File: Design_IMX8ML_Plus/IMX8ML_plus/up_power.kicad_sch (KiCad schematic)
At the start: 1 part, among them U1 MIMX8ML8CVNKZAB

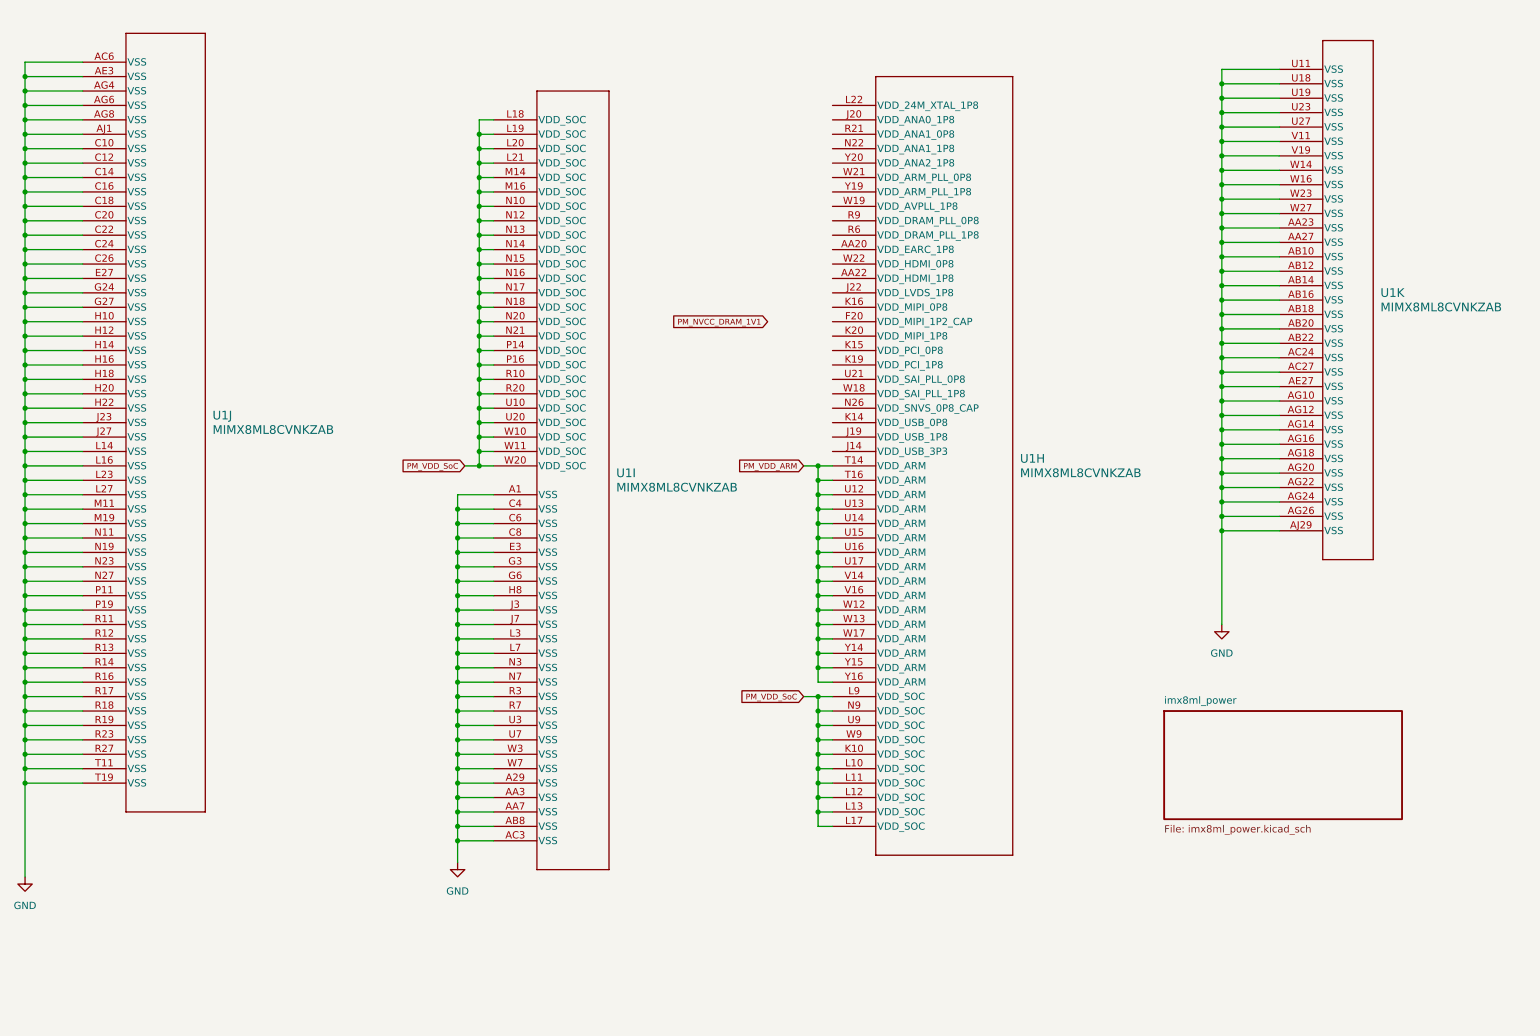
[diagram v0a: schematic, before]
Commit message: Add storage unit
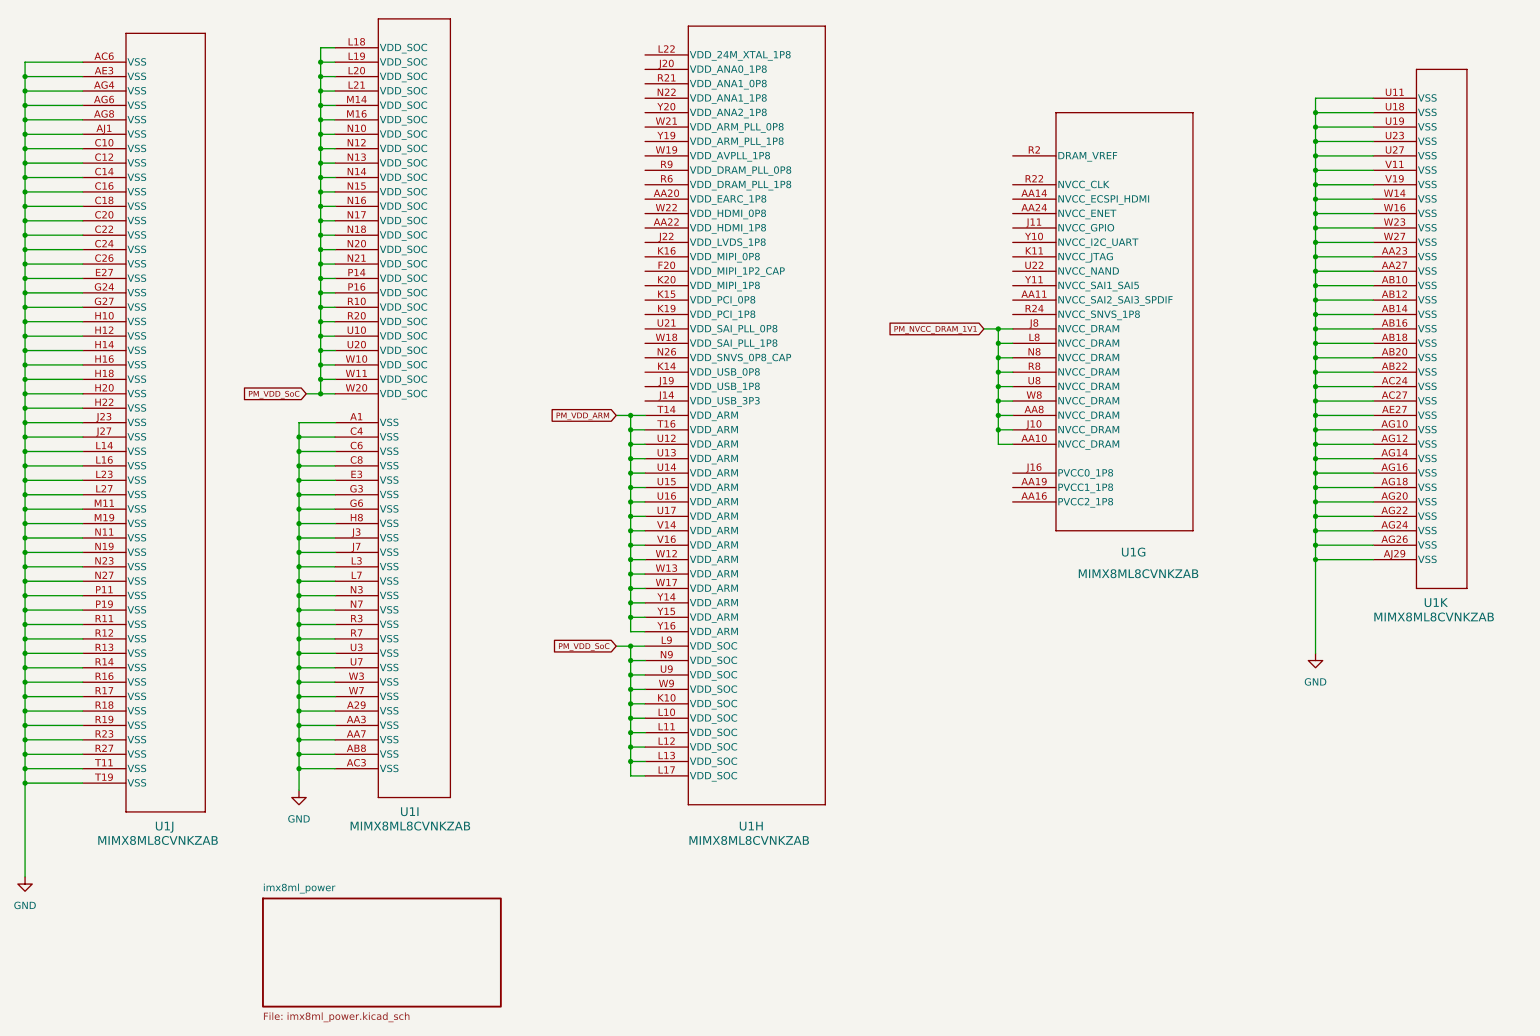
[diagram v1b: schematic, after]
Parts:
- added unit 7 of U1
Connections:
- net PM_NVCC_DRAM_1V1: now also U1.AA10 (NVCC_DRAM), U1.AA8 (NVCC_DRAM), U1.J10 (NVCC_DRAM), U1.J8 (NVCC_DRAM), U1.L8 (NVCC_DRAM), U1.N8 (NVCC_DRAM), U1.R8 (NVCC_DRAM), U1.U8 (NVCC_DRAM), U1.W8 (NVCC_DRAM)
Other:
- moved on the sheet: U1H, U1I, U1K

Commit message: Add interface io pins
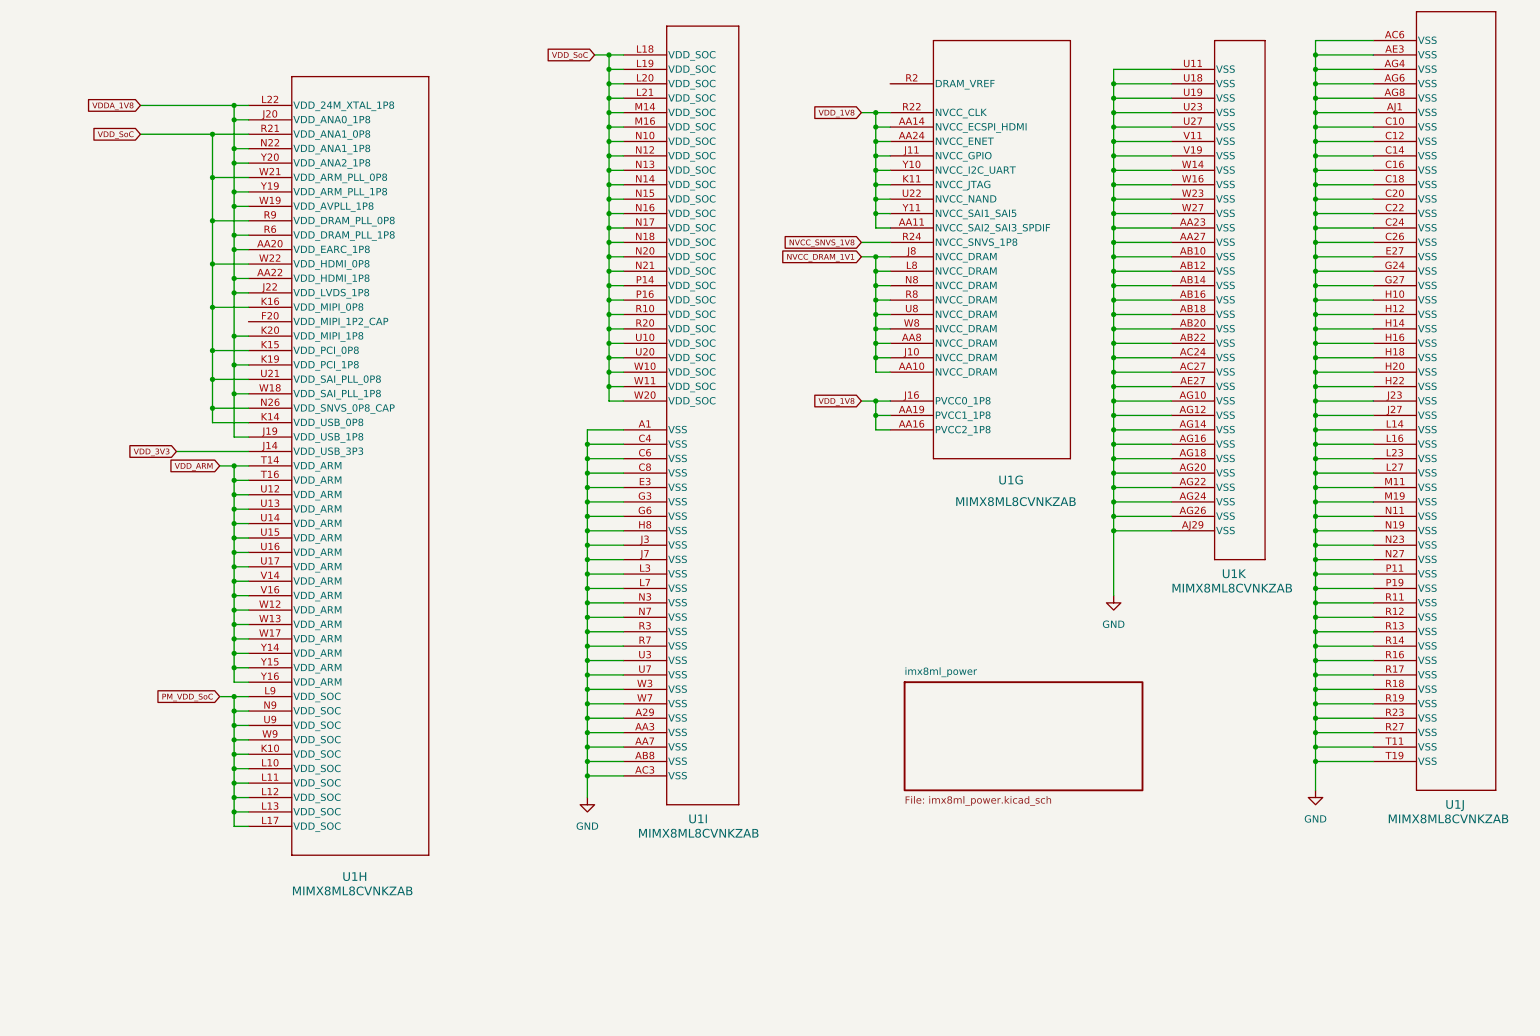
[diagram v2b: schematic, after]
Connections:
- net PM_VDD_SoC: no longer U1.L18 (VDD_SOC), U1.L19 (VDD_SOC), U1.L20 (VDD_SOC), U1.L21 (VDD_SOC), U1.M14 (VDD_SOC), U1.M16 (VDD_SOC), U1.N10 (VDD_SOC), U1.N12 (VDD_SOC), U1.N13 (VDD_SOC), U1.N14 (VDD_SOC), U1.N15 (VDD_SOC), U1.N16 (VDD_SOC), U1.N17 (VDD_SOC), U1.N18 (VDD_SOC), U1.N20 (VDD_SOC), U1.N21 (VDD_SOC), U1.P14 (VDD_SOC), U1.P16 (VDD_SOC), U1.R10 (VDD_SOC), U1.R20 (VDD_SOC), U1.U10 (VDD_SOC), U1.U20 (VDD_SOC), U1.W10 (VDD_SOC), U1.W11 (VDD_SOC), U1.W20 (VDD_SOC)
- net VDD_1V8: now reaches U1.AA11 (NVCC_SAI2_SAI3_SPDIF)
- net VDD_1V8: now also U1.AA14 (NVCC_ECSPI_HDMI), U1.AA16 (PVCC2_1P8), U1.AA19 (PVCC1_1P8), U1.AA24 (NVCC_ENET), U1.J11 (NVCC_GPIO), U1.J16 (PVCC0_1P8), U1.K11 (NVCC_JTAG), U1.R22 (NVCC_CLK), U1.U22 (NVCC_NAND), U1.Y10 (NVCC_I2C_UART), U1.Y11 (NVCC_SAI1_SAI5)
- net NVCC_SNVS_1V8: now reaches U1.R24 (NVCC_SNVS_1P8)
- net VDDA_1V8: now reaches U1.AA20 (VDD_EARC_1P8)
- net VDDA_1V8: now also U1.AA22 (VDD_HDMI_1P8), U1.J19 (VDD_USB_1P8), U1.J20 (VDD_ANA0_1P8), U1.J22 (VDD_LVDS_1P8), U1.K19 (VDD_PCI_1P8), U1.K20 (VDD_MIPI_1P8), U1.L22 (VDD_24M_XTAL_1P8), U1.N22 (VDD_ANA1_1P8), U1.R6 (VDD_DRAM_PLL_1P8), U1.W18 (VDD_SAI_PLL_1P8), U1.W19 (VDD_AVPLL_1P8), U1.Y19 (VDD_ARM_PLL_1P8), U1.Y20 (VDD_ANA2_1P8)
- net VDD_3V3: now reaches U1.J14 (VDD_USB_3P3)
- net VDD_SoC: now reaches U1.K14 (VDD_USB_0P8)
- net VDD_SoC: now also U1.K15 (VDD_PCI_0P8), U1.K16 (VDD_MIPI_0P8), U1.L18 (VDD_SOC), U1.L19 (VDD_SOC), U1.L20 (VDD_SOC), U1.L21 (VDD_SOC), U1.M14 (VDD_SOC), U1.M16 (VDD_SOC), U1.N10 (VDD_SOC), U1.N12 (VDD_SOC), U1.N13 (VDD_SOC), U1.N14 (VDD_SOC), U1.N15 (VDD_SOC), U1.N16 (VDD_SOC), U1.N17 (VDD_SOC), U1.N18 (VDD_SOC), U1.N20 (VDD_SOC), U1.N21 (VDD_SOC), U1.N26 (VDD_SNVS_0P8_CAP), U1.P14 (VDD_SOC), U1.P16 (VDD_SOC), U1.R10 (VDD_SOC), U1.R20 (VDD_SOC), U1.R21 (VDD_ANA1_0P8), U1.R9 (VDD_DRAM_PLL_0P8), U1.U10 (VDD_SOC), U1.U20 (VDD_SOC), U1.U21 (VDD_SAI_PLL_0P8), U1.W10 (VDD_SOC), U1.W11 (VDD_SOC), U1.W20 (VDD_SOC), U1.W21 (VDD_ARM_PLL_0P8), U1.W22 (VDD_HDMI_0P8)
- net PM_NVCC_DRAM_1V1 renamed NVCC_DRAM_1V1
- net PM_VDD_ARM renamed VDD_ARM
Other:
- moved on the sheet: U1G, U1H, U1I, U1J, U1K

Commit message: [PROCESSOR] Create zones It added power zones in the four layer
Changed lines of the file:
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@@
 	(wire
 		(pts
-			(xy 49.53 90.17) (xy 62.23 90.17)
+			(xy 57.15 90.17) (xy 62.23 90.17)
 		)
 		(stroke
@@
 	(global_label "VDD_3V3"
 		(shape input)
-		(at 49.53 90.17 180)
+		(at 57.15 90.17 180)
 		(fields_autoplaced yes)
 		(effects
@@
 		)
 		(property "Intersheetrefs" "${INTERSHEET_REFS}"
-			(at 40.8612 90.17 0)
+			(at 48.4812 90.17 0)
 			(effects
 				(font
@@
 		(dnp no)
 		(fields_autoplaced yes)
-		(property "Reference" "#PWR02"
+		(property "Reference" "#PWR3"
 			(at 250.19 156.21 0)
 			(effects
@@
 			(project "IMX8ML_plus"
 				(path "/1e0dca60-79b3-4b5b-ab8f-7b2adbc68a5f/c2b8be6d-439a-444c-a168-f4e9f22d3fc9/ff1e19bc-8af5-40c7-aebc-3ecef7e734aa"
-					(reference "#PWR02")
+					(reference "#PWR3")
 					(unit 1)
 				)
@@
 		(dnp no)
 		(fields_autoplaced yes)
-		(property "Reference" "#PWR03"
+		(property "Reference" "#PWR1"
 			(at 121.92 157.48 0)
 			(effects
@@
 			(project "IMX8ML_plus"
 				(path "/1e0dca60-79b3-4b5b-ab8f-7b2adbc68a5f/c2b8be6d-439a-444c-a168-f4e9f22d3fc9/ff1e19bc-8af5-40c7-aebc-3ecef7e734aa"
-					(reference "#PWR03")
+					(reference "#PWR1")
 					(unit 1)
 				)
@@
 		(dnp no)
 		(fields_autoplaced yes)
-		(property "Reference" "#PWR01"
+		(property "Reference" "#PWR2"
 			(at 214.63 121.92 0)
 			(effects
@@
 			(project "IMX8ML_plus"
 				(path "/1e0dca60-79b3-4b5b-ab8f-7b2adbc68a5f/c2b8be6d-439a-444c-a168-f4e9f22d3fc9/ff1e19bc-8af5-40c7-aebc-3ecef7e734aa"
-					(reference "#PWR01")
+					(reference "#PWR2")
 					(unit 1)
 				)

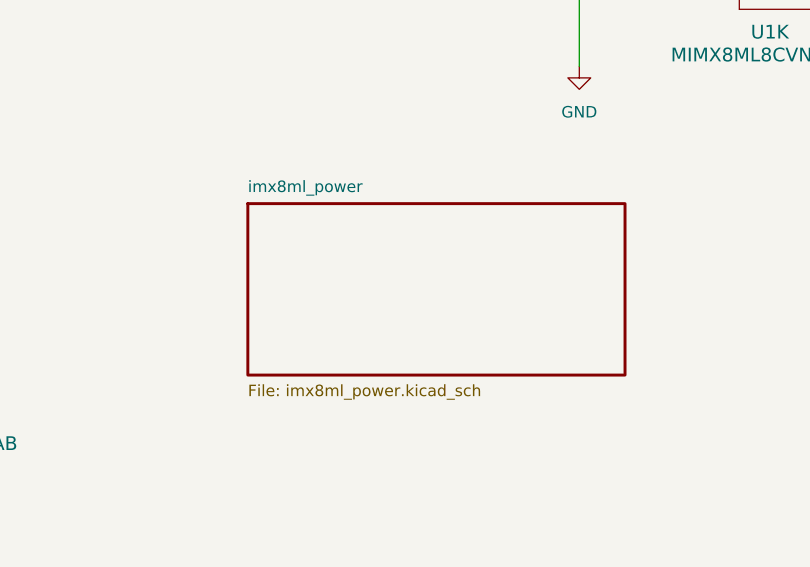
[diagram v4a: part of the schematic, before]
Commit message: [BB_IMX8MLP IMX8MLP] Actuallizated to 9.0 kicad version
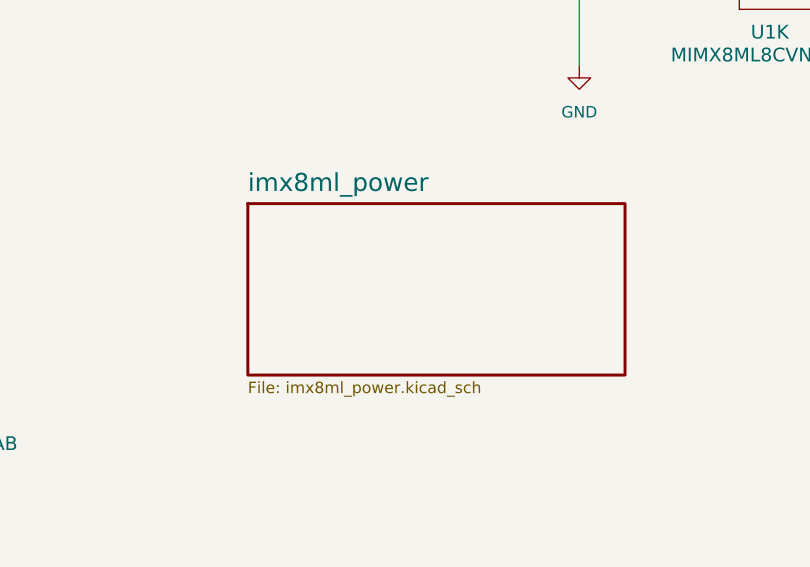
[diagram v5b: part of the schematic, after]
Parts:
- U1: footprint LFBGA548_SOT2047-1_NXP -> _W_SBC:LFBGA548_SOT2047-1_NXP; MP (none) -> -
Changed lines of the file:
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@@
 (kicad_sch
-	(version 20231120)
+	(version 20250114)
 	(generator "eeschema")
-	(generator_version "8.0")
+	(generator_version "9.0")
 	(paper "A4")
 	(junction
@@
 			)
 		)
-		(property "Footprint" "LFBGA548_SOT2047-1_NXP"
+		(property "Footprint" "_W_SBC:LFBGA548_SOT2047-1_NXP"
 			(at 265.43 22.86 0)
 			(effects
@@
 			)
 		)
+		(property "MP" "-"
+			(at 224.79 22.86 0)
+			(effects
+				(font
+					(size 1.27 1.27)
+				)
+				(hide yes)
+			)
+		)
 		(pin "F8"
 		)
@@
 			)
 		)
-		(property "Footprint" "LFBGA548_SOT2047-1_NXP"
+		(property "Footprint" "_W_SBC:LFBGA548_SOT2047-1_NXP"
 			(at 300.99 17.78 0)
 			(effects
@@
 			)
 		)
+		(property "MP" "-"
+			(at 260.35 17.78 0)
+			(effects
+				(font
+					(size 1.27 1.27)
+				)
+				(hide yes)
+			)
+		)
 		(pin "F8"
 		)
@@
 			)
 		)
-		(property "Footprint" "LFBGA548_SOT2047-1_NXP"
+		(property "Footprint" "_W_SBC:LFBGA548_SOT2047-1_NXP"
 			(at 215.9 25.4 0)
 			(effects
@@
 			)
 		)
+		(property "MP" "-"
+			(at 175.26 25.4 0)
+			(effects
+				(font
+					(size 1.27 1.27)
+				)
+				(hide yes)
+			)
+		)
 		(pin "F8"
 		)
@@
 			)
 		)
-		(property "Footprint" "LFBGA548_SOT2047-1_NXP"
+		(property "Footprint" "_W_SBC:LFBGA548_SOT2047-1_NXP"
 			(at 102.87 29.21 0)
 			(effects
@@
 			)
 		)
+		(property "MP" "-"
+			(at 62.23 29.21 0)
+			(effects
+				(font
+					(size 1.27 1.27)
+				)
+				(hide yes)
+			)
+		)
 		(pin "F8"
 		)
@@
 			)
 		)
-		(property "Footprint" "LFBGA548_SOT2047-1_NXP"
+		(property "Footprint" "_W_SBC:LFBGA548_SOT2047-1_NXP"
 			(at 168.91 20.32 0)
 			(effects
@@
 			)
 		)
+		(property "MP" "-"
+			(at 128.27 20.32 0)
+			(effects
+				(font
+					(size 1.27 1.27)
+				)
+				(hide yes)
+			)
+		)
 		(pin "F8"
 		)
@@
 		(at 177.8 130.81)
 		(size 41.91 19.05)
+		(exclude_from_sim no)
+		(in_bom yes)
+		(on_board yes)
+		(dnp no)
 		(fields_autoplaced yes)
 		(stroke
@@
 		)
 		(property "Sheetname" "imx8ml_power"
-			(at 177.8 129.6746 0)
+			(at 177.8 129.6461 0)
 			(effects
 				(font
-					(size 1.27 1.27)
+					(size 2 2)
 				)
 				(justify left bottom)
@@
 		)
 		(property "Sheetfile" "imx8ml_power.kicad_sch"
-			(at 177.8 150.8684 0)
+			(at 177.8 150.5319 0)
 			(effects
 				(font
